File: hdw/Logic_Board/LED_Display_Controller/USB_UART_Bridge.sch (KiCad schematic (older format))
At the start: 30 parts, among them J1101 USB_B_Mini, U1101 LT6700-1-S6, U1102 FT234XD, U1103 74LVC1G06, U1104 TPD3S014DBVR

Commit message: Added to do list iem
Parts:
- J1101: footprint (none) -> Connectors:USB_Mini-B
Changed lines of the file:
@@
 F 0 "J1101" H 8681 3281 50  0000 R CNN
 F 1 "USB_B_Mini" H 8681 3190 50  0000 R CNN
-F 2 "" H 9060 3240 50  0001 C CNN
+F 2 "Connectors:USB_Mini-B" H 9060 3240 50  0001 C CNN
 F 3 "~" H 9060 3240 50  0001 C CNN
 	1    8910 3290

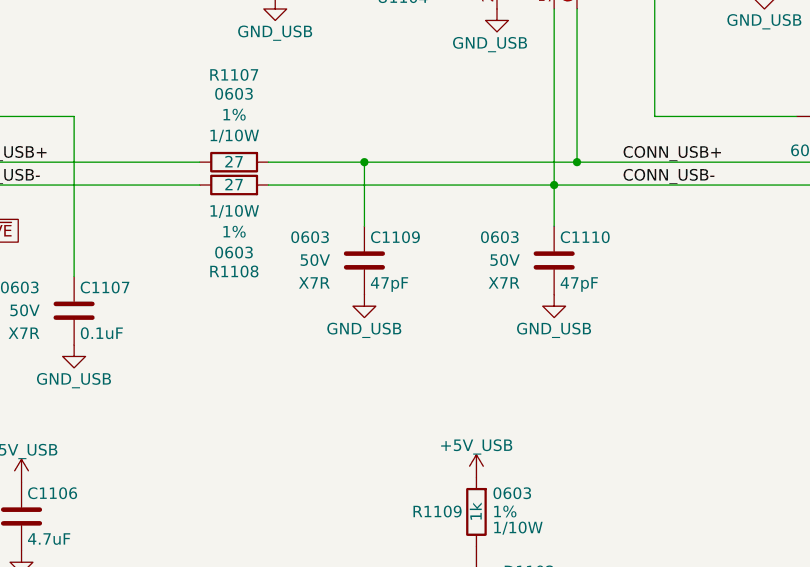
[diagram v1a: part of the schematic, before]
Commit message: Added some digikey partnumbers to components
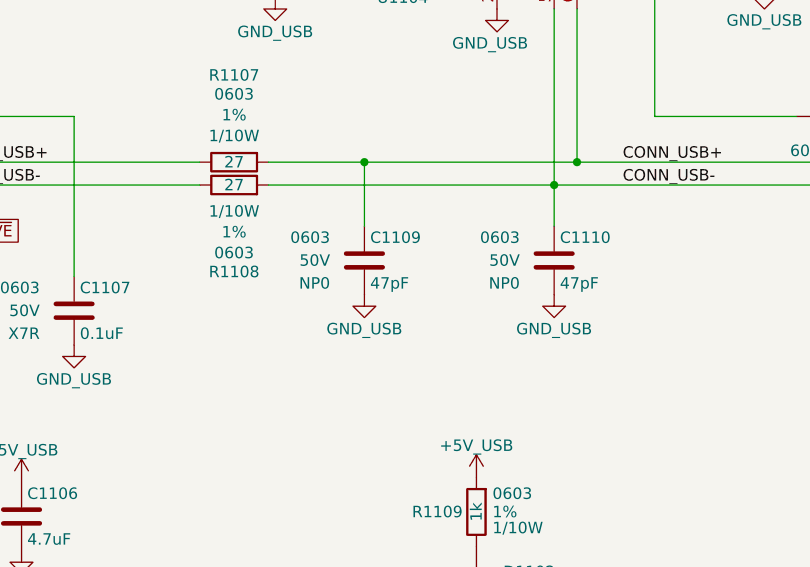
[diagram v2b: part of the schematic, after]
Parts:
- C1101, C1102, C1103, C1104, C1105, C1107, C1108, C1111: footprint (none) -> Capacitors_SMD:C_0603; Digi-Key PN PN -> 311-1344-1-ND
- C1106: Digi-Key PN PN -> 1276-2972-1-ND
- C1109, C1110: Dielectric X7R -> NP0; Digi-Key PN PN -> 478-1171-1-ND
- D1101: Digi-Key PN (none) -> 160-1446-1-ND
- D1102: Digi-Key PN (none) -> 160-1448-1-ND
- J1101: Digi-Key PN (none) -> 732-2109-1-ND
- L1101, L1102: Digi-Key PN (none) -> 732-2389-1-ND
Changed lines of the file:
@@
 F 4 "0603" H 6000 3820 50  0000 R CNN "display_footprint"
 F 5 "50V" H 6000 3720 50  0000 R CNN "Voltage"
-F 6 "X7R" H 6000 3620 50  0000 R CNN "Dielectric"
-F 7 "PN" H 6575 4220 60  0001 C CNN "Digi-Key PN"
+F 6 "NP0" H 6000 3620 50  0000 R CNN "Dielectric"
+F 7 "478-1171-1-ND" H 6575 4220 60  0001 C CNN "Digi-Key PN"
 	1    6150 3720
 	1    0    0    -1
@@
 F 0 "C1104" H 3995 4940 50  0000 L CNN
 F 1 "0.1uF" H 3995 4740 50  0000 L CNN
-F 2 "" H 4008 4690 50  0001 C CNN
+F 2 "Capacitors_SMD:C_0603" H 4008 4690 50  0001 C CNN
 F 3 "" H 3995 4940 50  0001 C CNN
 F 4 "0603" H 3820 4940 50  0000 R CNN "display_footprint"
 F 5 "50V" H 3820 4840 50  0000 R CNN "Voltage"
 F 6 "X7R" H 3820 4740 50  0000 R CNN "Dielectric"
-F 7 "PN" H 4395 5340 60  0001 C CNN "Digi-Key PN"
+F 7 "311-1344-1-ND" H 4395 5340 60  0001 C CNN "Digi-Key PN"
 	1    3970 4840
 	1    0    0    -1
@@
 F 5 "10V" H 4500 4840 50  0000 R CNN "Voltage"
 F 6 "X7R" H 4500 4740 50  0000 R CNN "Dielectric"
-F 7 "PN" H 5075 5340 60  0001 C CNN "Digi-Key PN"
+F 7 "1276-2972-1-ND" H 5075 5340 60  0001 C CNN "Digi-Key PN"
 	1    4650 4840
 	1    0    0    -1
@@
 F 0 "C1101" H 1535 3930 50  0000 L CNN
 F 1 "0.1uF" H 1535 3730 50  0000 L CNN
-F 2 "" H 1548 3680 50  0001 C CNN
+F 2 "Capacitors_SMD:C_0603" H 1548 3680 50  0001 C CNN
 F 3 "" H 1535 3930 50  0001 C CNN
 F 4 "0603" H 1360 3930 50  0000 R CNN "display_footprint"
 F 5 "50V" H 1360 3830 50  0000 R CNN "Voltage"
 F 6 "X7R" H 1360 3730 50  0000 R CNN "Dielectric"
-F 7 "PN" H 1935 4330 60  0001 C CNN "Digi-Key PN"
+F 7 "311-1344-1-ND" H 1935 4330 60  0001 C CNN "Digi-Key PN"
 	1    1510 3830
 	1    0    0    -1
@@
 F 4 "0603" H 6830 3820 50  0000 R CNN "display_footprint"
 F 5 "50V" H 6830 3720 50  0000 R CNN "Voltage"
-F 6 "X7R" H 6830 3620 50  0000 R CNN "Dielectric"
-F 7 "PN" H 7405 4220 60  0001 C CNN "Digi-Key PN"
+F 6 "NP0" H 6830 3620 50  0000 R CNN "Dielectric"
+F 7 "478-1171-1-ND" H 7405 4220 60  0001 C CNN "Digi-Key PN"
 	1    6980 3720
 	1    0    0    -1
@@
 F 0 "C1102" H 3305 4940 50  0000 L CNN
 F 1 "0.1uF" H 3305 4740 50  0000 L CNN
-F 2 "" H 3318 4690 50  0001 C CNN
+F 2 "Capacitors_SMD:C_0603" H 3318 4690 50  0001 C CNN
 F 3 "" H 3305 4940 50  0001 C CNN
 F 4 "0603" H 3130 4940 50  0000 R CNN "display_footprint"
 F 5 "50V" H 3130 4840 50  0000 R CNN "Voltage"
 F 6 "X7R" H 3130 4740 50  0000 R CNN "Dielectric"
-F 7 "PN" H 3705 5340 60  0001 C CNN "Digi-Key PN"
+F 7 "311-1344-1-ND" H 3705 5340 60  0001 C CNN "Digi-Key PN"
 	1    3280 4840
 	1    0    0    -1
@@
 F 0 "C1107" H 4905 4040 50  0000 L CNN
 F 1 "0.1uF" H 4905 3840 50  0000 L CNN
-F 2 "" H 4918 3790 50  0001 C CNN
+F 2 "Capacitors_SMD:C_0603" H 4918 3790 50  0001 C CNN
 F 3 "" H 4905 4040 50  0001 C CNN
 F 4 "0603" H 4730 4040 50  0000 R CNN "display_footprint"
 F 5 "50V" H 4730 3940 50  0000 R CNN "Voltage"
 F 6 "X7R" H 4730 3840 50  0000 R CNN "Dielectric"
-F 7 "PN" H 5305 4440 60  0001 C CNN "Digi-Key PN"
+F 7 "311-1344-1-ND" H 5305 4440 60  0001 C CNN "Digi-Key PN"
 	1    4880 3940
 	1    0    0    -1
@@
 F 0 "C1111" H 7925 2470 50  0000 L CNN
 F 1 "0.1uF" H 7925 2270 50  0000 L CNN
-F 2 "" H 7938 2220 50  0001 C CNN
+F 2 "Capacitors_SMD:C_0603" H 7938 2220 50  0001 C CNN
 F 3 "" H 7925 2470 50  0001 C CNN
 F 4 "0603" H 7750 2470 50  0000 R CNN "display_footprint"
 F 5 "50V" H 7750 2370 50  0000 R CNN "Voltage"
 F 6 "X7R" H 7750 2270 50  0000 R CNN "Dielectric"
-F 7 "PN" H 8325 2870 60  0001 C CNN "Digi-Key PN"
+F 7 "311-1344-1-ND" H 8325 2870 60  0001 C CNN "Digi-Key PN"
 	1    7900 2370
 	1    0    0    -1
@@
 F 0 "C1108" H 5785 2520 50  0000 L CNN
 F 1 "0.1uF" H 5785 2320 50  0000 L CNN
-F 2 "" H 5798 2270 50  0001 C CNN
+F 2 "Capacitors_SMD:C_0603" H 5798 2270 50  0001 C CNN
 F 3 "" H 5785 2520 50  0001 C CNN
 F 4 "0603" H 5610 2520 50  0000 R CNN "display_footprint"
 F 5 "50V" H 5610 2420 50  0000 R CNN "Voltage"
 F 6 "X7R" H 5610 2320 50  0000 R CNN "Dielectric"
-F 7 "PN" H 6185 2920 60  0001 C CNN "Digi-Key PN"
+F 7 "311-1344-1-ND" H 6185 2920 60  0001 C CNN "Digi-Key PN"
 	1    5760 2420
 	1    0    0    -1
@@
 F 2 "" V 8120 3090 50  0001 C CNN
 F 3 "~" H 8190 3090 50  0001 C CNN
+F 4 "732-2389-1-ND" H 0   0   50  0001 C CNN "Digi-Key PN"
 	1    8190 3090
 	0    1    1    0
@@
 F 2 "" H 6640 5120 50  0001 C CNN
 F 3 "~" H 6640 5120 50  0001 C CNN
+F 4 "160-1448-1-ND" H 0   0   50  0001 C CNN "Digi-Key PN"
 	1    6640 5120
 	0    -1   -1   0
@@
 F 2 "Connectors:USB_Mini-B" H 9060 3240 50  0001 C CNN
 F 3 "~" H 9060 3240 50  0001 C CNN
+F 4 "732-2109-1-ND" H 0   0   50  0001 C CNN "Digi-Key PN"
 	1    8910 3290
 	-1   0    0    -1
@@
 F 2 "" V 9460 3760 50  0001 C CNN
 F 3 "~" H 9530 3760 50  0001 C CNN
+F 4 "732-2389-1-ND" H 0   0   50  0001 C CNN "Digi-Key PN"
 	1    9530 3760
 	0    1    1    0
@@
 F 0 "C1105" H 4465 7410 50  0000 L CNN
 F 1 "0.1uF" H 4465 7210 50  0000 L CNN
-F 2 "" H 4478 7160 50  0001 C CNN
+F 2 "Capacitors_SMD:C_0603" H 4478 7160 50  0001 C CNN
 F 3 "" H 4465 7410 50  0001 C CNN
-F 4 "PN" H 4865 7810 60  0001 C CNN "Digi-Key PN"
+F 4 "311-1344-1-ND" H 4865 7810 60  0001 C CNN "Digi-Key PN"
 F 5 "0603" H 4290 7410 50  0000 R CNN "display_footprint"
 F 6 "50V" H 4290 7310 50  0000 R CNN "Voltage"
@@
 F 2 "" H 5160 6320 50  0001 C CNN
 F 3 "~" H 5160 6320 50  0001 C CNN
+F 4 "160-1446-1-ND" H 0   0   50  0001 C CNN "Digi-Key PN"
 	1    5160 6320
 	0    -1   -1   0
@@
 F 0 "C1103" H 3565 7650 50  0000 L CNN
 F 1 "0.1uF" H 3565 7450 50  0000 L CNN
-F 2 "" H 3578 7400 50  0001 C CNN
+F 2 "Capacitors_SMD:C_0603" H 3578 7400 50  0001 C CNN
 F 3 "" H 3565 7650 50  0001 C CNN
-F 4 "PN" H 3965 8050 60  0001 C CNN "Digi-Key PN"
+F 4 "311-1344-1-ND" H 3965 8050 60  0001 C CNN "Digi-Key PN"
 F 5 "0603" H 3390 7650 50  0000 R CNN "display_footprint"
 F 6 "50V" H 3390 7550 50  0000 R CNN "Voltage"

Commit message: Finished first pass of digikey part numbers
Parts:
- R1101, R1105: Digi-Key PN PN -> RMCF0603FT10K0CT-ND
- R1102: Digi-Key PN PN -> 311-487KHRCT-ND
- R1103: Digi-Key PN PN -> RMCF0603FT6K04CT-ND
- R1104: Digi-Key PN PN -> 311-40.2KHRCT-ND
- R1106, R1109: Digi-Key PN PN -> RMCF0603FT1K00CT-ND
- R1107, R1108: Digi-Key PN PN -> RMCF0603FT27R0CT-ND
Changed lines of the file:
@@
 F 5 "1%" H 1610 3400 50  0000 L CNN "Tolerance"
 F 6 "1/10W" H 1620 3320 50  0000 L CNN "Wattage"
-F 7 "PN" H 1810 3800 60  0001 C CNN "Digi-Key PN"
+F 7 "RMCF0603FT10K0CT-ND" H 1810 3800 60  0001 C CNN "Digi-Key PN"
 	1    1510 3400
 	1    0    0    -1
@@
 F 5 "1%" H 6710 4820 50  0000 L CNN "Tolerance"
 F 6 "1/10W" H 6710 4750 50  0000 L CNN "Wattage"
-F 7 "PN" H 6940 5220 60  0001 C CNN "Digi-Key PN"
+F 7 "RMCF0603FT1K00CT-ND" H 6940 5220 60  0001 C CNN "Digi-Key PN"
 	1    6640 4820
 	1    0    0    -1
@@
 F 5 "1%" V 5786 3290 50  0000 C CNN "Tolerance"
 F 6 "1/10W" V 5695 3290 50  0000 C CNN "Wattage"
-F 7 "PN" H 5880 3690 60  0001 C CNN "Digi-Key PN"
+F 7 "RMCF0603FT27R0CT-ND" H 5880 3690 60  0001 C CNN "Digi-Key PN"
 	1    5580 3290
 	0    1    -1   0
@@
 F 5 "1%" H 1940 6830 50  0000 L CNN "Tolerance"
 F 6 "1/10W" H 1950 6750 50  0000 L CNN "Wattage"
-F 7 "PN" H 2140 7230 60  0001 C CNN "Digi-Key PN"
+F 7 "RMCF0603FT6K04CT-ND" H 2140 7230 60  0001 C CNN "Digi-Key PN"
 	1    1840 6830
 	1    0    0    -1
@@
 F 5 "1%" H 1940 7320 50  0000 L CNN "Tolerance"
 F 6 "1/10W" H 1950 7240 50  0000 L CNN "Wattage"
-F 7 "PN" H 2140 7720 60  0001 C CNN "Digi-Key PN"
+F 7 "311-40.2KHRCT-ND" H 2140 7720 60  0001 C CNN "Digi-Key PN"
 	1    1840 7320
 	1    0    0    -1
@@
 F 5 "1%" H 1940 6290 50  0000 L CNN "Tolerance"
 F 6 "1/10W" H 1950 6210 50  0000 L CNN "Wattage"
-F 7 "PN" H 2140 6690 60  0001 C CNN "Digi-Key PN"
+F 7 "311-487KHRCT-ND" H 2140 6690 60  0001 C CNN "Digi-Key PN"
 	1    1840 6290
 	1    0    0    -1
@@
 F 5 "1%" H 3570 6240 50  0000 L CNN "Tolerance"
 F 6 "1/10W" H 3580 6160 50  0000 L CNN "Wattage"
-F 7 "PN" H 3770 6640 60  0001 C CNN "Digi-Key PN"
+F 7 "RMCF0603FT10K0CT-ND" H 3770 6640 60  0001 C CNN "Digi-Key PN"
 	1    3470 6240
 	1    0    0    -1
@@
 F 5 "1%" H 5230 6020 50  0000 L CNN "Tolerance"
 F 6 "1/10W" H 5240 5950 50  0000 L CNN "Wattage"
-F 7 "PN" H 5460 6420 60  0001 C CNN "Digi-Key PN"
+F 7 "RMCF0603FT1K00CT-ND" H 5460 6420 60  0001 C CNN "Digi-Key PN"
 	1    5160 6020
 	-1   0    0    -1
@@
 F 5 "1%" V 5786 3390 50  0000 C CNN "Tolerance"
 F 6 "1/10W" V 5695 3390 50  0000 C CNN "Wattage"
-F 7 "PN" H 5880 3790 60  0001 C CNN "Digi-Key PN"
+F 7 "RMCF0603FT27R0CT-ND" H 5880 3790 60  0001 C CNN "Digi-Key PN"
 	1    5580 3390
 	0    1    1    0

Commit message: First pass assignment of footprints to all components
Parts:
- C1106: footprint (none) -> Capacitors_SMD:C_0805
- C1109, C1110: footprint (none) -> Capacitors_SMD:C_0603
- D1101, D1102: footprint (none) -> LEDs:LED_0603
- L1101, L1102: footprint (none) -> Inductors_SMD:L_0603
- R1101, R1102, R1103, R1104, R1105, R1106, R1107, R1108, R1109: footprint (none) -> Resistors_SMD:R_0603
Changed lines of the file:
@@
 F 0 "C1109" H 6175 3820 50  0000 L CNN
 F 1 "47pF" H 6175 3620 50  0000 L CNN
-F 2 "" H 6188 3570 50  0001 C CNN
+F 2 "Capacitors_SMD:C_0603" H 6188 3570 50  0001 C CNN
 F 3 "" H 6175 3820 50  0001 C CNN
 F 4 "0603" H 6000 3820 50  0000 R CNN "display_footprint"
@@
 F 0 "C1106" H 4675 4940 50  0000 L CNN
 F 1 "4.7uF" H 4675 4740 50  0000 L CNN
-F 2 "" H 4688 4690 50  0001 C CNN
+F 2 "Capacitors_SMD:C_0805" H 4688 4690 50  0001 C CNN
 F 3 "" H 4675 4940 50  0001 C CNN
 F 4 "0805" H 4500 4940 50  0000 R CNN "display_footprint"
@@
 F 0 "R1101" H 1450 3400 50  0000 R CNN
 F 1 "10k" V 1510 3400 50  0000 C CNN
-F 2 "" H 1510 3400 50  0001 C CNN
+F 2 "Resistors_SMD:R_0603" H 1510 3400 50  0001 C CNN
 F 3 "" H 1510 3400 50  0001 C CNN
 F 4 "0603" H 1610 3490 50  0000 L CNN "display_footprint"
@@
 F 0 "C1110" H 7005 3820 50  0000 L CNN
 F 1 "47pF" H 7005 3620 50  0000 L CNN
-F 2 "" H 7018 3570 50  0001 C CNN
+F 2 "Capacitors_SMD:C_0603" H 7018 3570 50  0001 C CNN
 F 3 "" H 7005 3820 50  0001 C CNN
 F 4 "0603" H 6830 3820 50  0000 R CNN "display_footprint"
@@
 F 0 "R1109" H 6580 4820 50  0000 R CNN
 F 1 "1k" V 6640 4820 50  0000 C CNN
-F 2 "" H 6640 4820 50  0001 C CNN
+F 2 "Resistors_SMD:R_0603" H 6640 4820 50  0001 C CNN
 F 3 "" H 6640 4820 50  0001 C CNN
 F 4 "0603" H 6710 4900 50  0000 L CNN "display_footprint"
@@
 F 0 "L1101" V 8040 3115 50  0000 C CNN
 F 1 "600R 0.5A" V 8340 3090 50  0000 C CNN
-F 2 "" V 8120 3090 50  0001 C CNN
+F 2 "Inductors_SMD:L_0603" V 8120 3090 50  0001 C CNN
 F 3 "~" H 8190 3090 50  0001 C CNN
 F 4 "732-2389-1-ND" H 0   0   50  0001 C CNN "Digi-Key PN"
@@
 F 0 "R1107" V 5960 3290 50  0000 C CNN
 F 1 "27" V 5580 3290 50  0000 C CNN
-F 2 "" H 5580 3290 50  0001 C CNN
+F 2 "Resistors_SMD:R_0603" H 5580 3290 50  0001 C CNN
 F 3 "" H 5580 3290 50  0001 C CNN
 F 4 "0603" V 5877 3290 50  0000 C CNN "display_footprint"
@@
 F 0 "D1102" V 6678 5003 50  0000 R CNN
 F 1 "Yellow" V 6587 5003 50  0000 R CNN
-F 2 "" H 6640 5120 50  0001 C CNN
+F 2 "LEDs:LED_0603" H 6640 5120 50  0001 C CNN
 F 3 "~" H 6640 5120 50  0001 C CNN
 F 4 "160-1448-1-ND" H 0   0   50  0001 C CNN "Digi-Key PN"
@@
 F 0 "L1102" V 9380 3785 50  0000 C CNN
 F 1 "600R 0.5A" V 9680 3760 50  0000 C CNN
-F 2 "" V 9460 3760 50  0001 C CNN
+F 2 "Inductors_SMD:L_0603" V 9460 3760 50  0001 C CNN
 F 3 "~" H 9530 3760 50  0001 C CNN
 F 4 "732-2389-1-ND" H 0   0   50  0001 C CNN "Digi-Key PN"
@@
 F 0 "R1103" H 1780 6830 50  0000 R CNN
 F 1 "6.04k" V 1840 6830 40  0000 C CNN
-F 2 "" H 1840 6830 50  0001 C CNN
+F 2 "Resistors_SMD:R_0603" H 1840 6830 50  0001 C CNN
 F 3 "" H 1840 6830 50  0001 C CNN
 F 4 "0603" H 1940 6920 50  0000 L CNN "display_footprint"
@@
 F 0 "R1104" H 1780 7320 50  0000 R CNN
 F 1 "40.2k" V 1840 7320 40  0000 C CNN
-F 2 "" H 1840 7320 50  0001 C CNN
+F 2 "Resistors_SMD:R_0603" H 1840 7320 50  0001 C CNN
 F 3 "" H 1840 7320 50  0001 C CNN
 F 4 "0603" H 1940 7410 50  0000 L CNN "display_footprint"
@@
 F 0 "R1102" H 1780 6290 50  0000 R CNN
 F 1 "487k" V 1840 6290 40  0000 C CNN
-F 2 "" H 1840 6290 50  0001 C CNN
+F 2 "Resistors_SMD:R_0603" H 1840 6290 50  0001 C CNN
 F 3 "" H 1840 6290 50  0001 C CNN
 F 4 "0603" H 1940 6380 50  0000 L CNN "display_footprint"
@@
 F 0 "R1105" H 3410 6240 50  0000 R CNN
 F 1 "10k" V 3470 6240 50  0000 C CNN
-F 2 "" H 3470 6240 50  0001 C CNN
+F 2 "Resistors_SMD:R_0603" H 3470 6240 50  0001 C CNN
 F 3 "" H 3470 6240 50  0001 C CNN
 F 4 "0603" H 3570 6330 50  0000 L CNN "display_footprint"
@@
 F 0 "D1101" V 5198 6203 50  0000 R CNN
 F 1 "Green" V 5107 6203 50  0000 R CNN
-F 2 "" H 5160 6320 50  0001 C CNN
+F 2 "LEDs:LED_0603" H 5160 6320 50  0001 C CNN
 F 3 "~" H 5160 6320 50  0001 C CNN
 F 4 "160-1446-1-ND" H 0   0   50  0001 C CNN "Digi-Key PN"
@@
 F 0 "R1106" H 5100 6020 50  0000 R CNN
 F 1 "1k" V 5160 6020 50  0000 C CNN
-F 2 "" H 5160 6020 50  0001 C CNN
+F 2 "Resistors_SMD:R_0603" H 5160 6020 50  0001 C CNN
 F 3 "" H 5160 6020 50  0001 C CNN
 F 4 "0603" H 5230 6100 50  0000 L CNN "display_footprint"
@@
 F 0 "R1108" V 5960 3390 50  0000 C CNN
 F 1 "27" V 5580 3390 50  0000 C CNN
-F 2 "" H 5580 3390 50  0001 C CNN
+F 2 "Resistors_SMD:R_0603" H 5580 3390 50  0001 C CNN
 F 3 "" H 5580 3390 50  0001 C CNN
 F 4 "0603" V 5877 3390 50  0000 C CNN "display_footprint"

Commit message: Modified BOM
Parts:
- U1101: Digi-Key PN LT6700IS6-1#TRMPBFCT-ND -> LT6700CS6-1#TRMPBFCT-ND
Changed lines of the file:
@@
 F 2 "TO_SOT_Packages_SMD:TSOT-23-6" H 2790 6840 60  0001 C CNN
 F 3 "http://www.analog.com/media/en/technical-documentation/data-sheets/6700123fh.pdf" H 2790 6840 60  0001 C CNN
-F 4 "LT6700IS6-1#TRMPBFCT-ND" H 2790 6840 50  0001 C CNN "Digi-Key PN"
+F 4 "LT6700CS6-1#TRMPBFCT-ND" H 2790 6840 50  0001 C CNN "Digi-Key PN"
 	1    2790 6840
 	1    0    0    -1
